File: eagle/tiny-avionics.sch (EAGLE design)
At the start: 60 parts, among them J1 USB-MICROB, J3 JST-PH-2-SMT-RA, U1 LP5907, U5 LTC1998, U6 ATMEGA32U4-AU, X1 8MHz

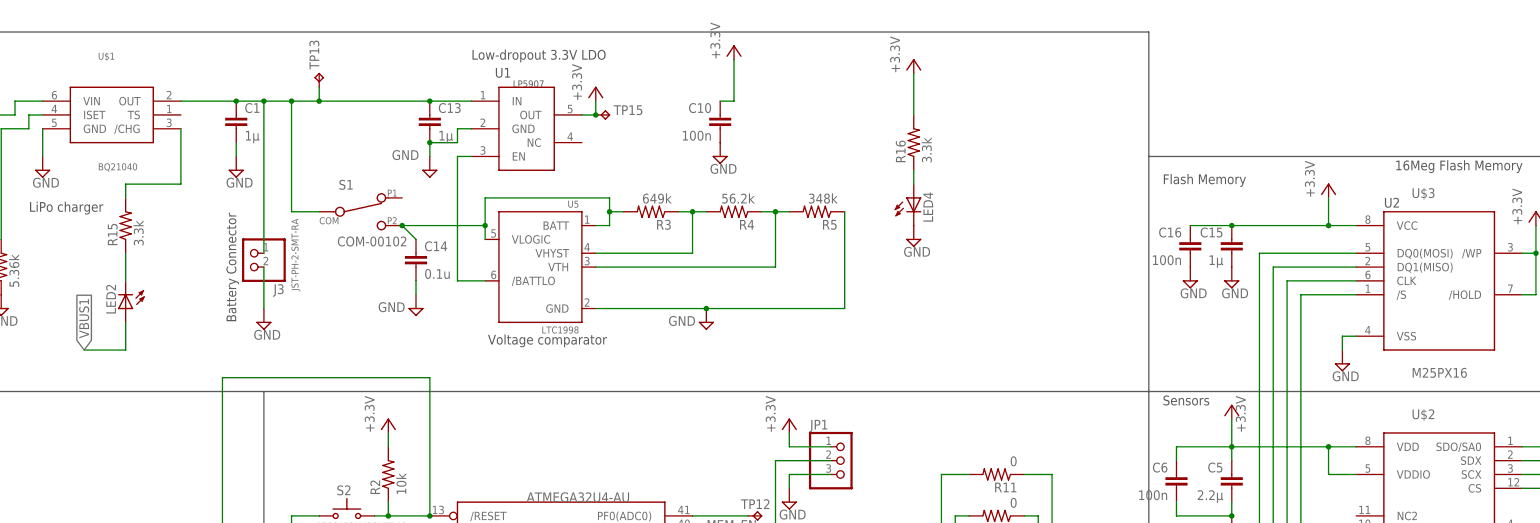
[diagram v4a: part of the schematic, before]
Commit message: Finished new board layout with no DRC errors.
It's a little smaller, but not much smaller.  Made an effort to spread out
components for easier assembly, however.  Layout is also much more
intuitive.
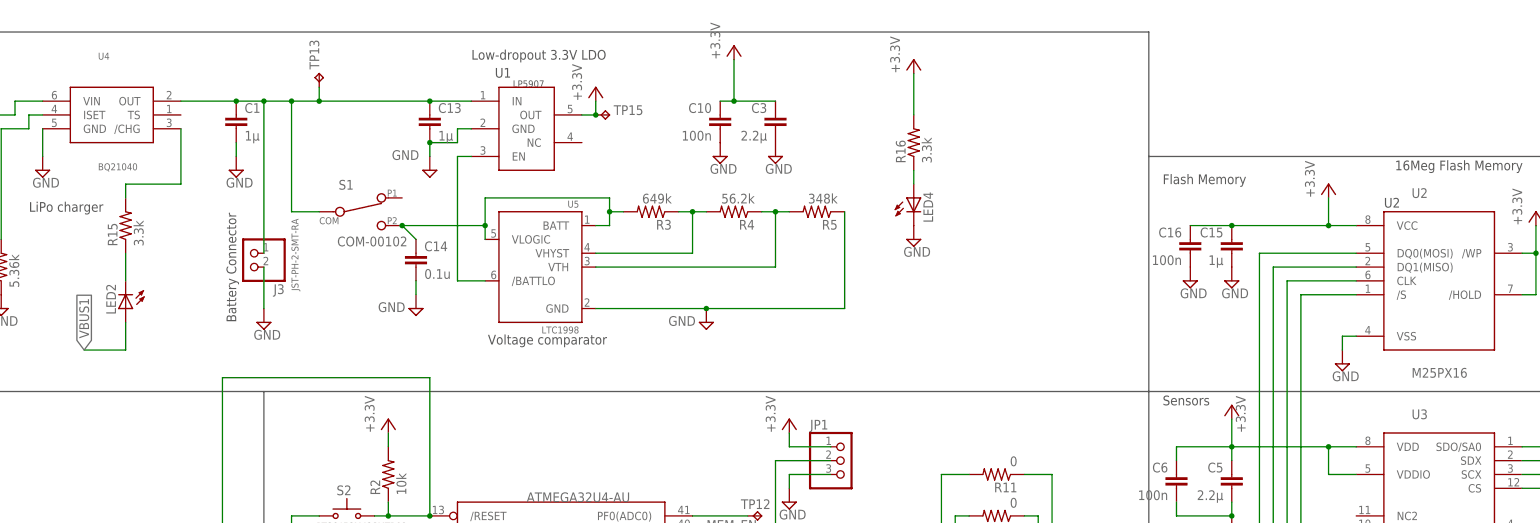
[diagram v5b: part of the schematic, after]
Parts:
- added C3: 2.2µ, rcl:C-EUC0603
- renumbered U$1 to U4, U$2 to U3, U$3 to U2
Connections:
- net GND: now also C3.2
- net VCC: now also C3.1
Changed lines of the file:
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@@
 <part name="TP15" library="testpad" deviceset="TP" device="TP08R"/>
 <part name="R17" library="rcl" deviceset="R-US_" device="R0603" value="0"/>
-<part name="U$1" library="tinyav-lib" deviceset="BQ21040" device=""/>
+<part name="U4" library="tinyav-lib" deviceset="BQ21040" device=""/>
 <part name="SUPPLY1" library="supply2" deviceset="GND" device=""/>
 <part name="R1" library="rcl" deviceset="R-US_" device="R0603" value="5.36k"/>
 <part name="SUPPLY3" library="supply2" deviceset="GND" device=""/>
-<part name="U$2" library="tinyav-lib" deviceset="LSM6DS3" device=""/>
+<part name="U3" library="tinyav-lib" deviceset="LSM6DS3" device=""/>
 <part name="SUPPLY7" library="supply2" deviceset="GND" device=""/>
 <part name="SUPPLY9" library="supply2" deviceset="GND" device=""/>
-<part name="U$3" library="tinyav-lib" deviceset="M25PX16" device=""/>
+<part name="U2" library="tinyav-lib" deviceset="M25PX16" device=""/>
 <part name="P+11" library="supply1" deviceset="VCC" device="" value="+3.3V"/>
 <part name="SUPPLY10" library="supply2" deviceset="GND" device=""/>
+<part name="C3" library="rcl" deviceset="C-EU" device="C0603" value="2.2µ"/>
+<part name="SUPPLY14" library="supply2" deviceset="GND" device=""/>
 </parts>
 <sheets>
@@
 <attribute name="VALUE" x="180.848" y="156.972" size="1.778" layer="96" rot="R180"/>
 </instance>
-<instance part="U$1" gate="BQ21040" x="68.58" y="248.92"/>
+<instance part="U4" gate="BQ21040" x="68.58" y="248.92"/>
 <instance part="SUPPLY1" gate="GND" x="55.88" y="238.76"/>
 <instance part="R1" gate="G$1" x="48.26" y="220.98" rot="R90"/>
 <instance part="SUPPLY3" gate="GND" x="48.26" y="213.36"/>
-<instance part="U$2" gate="G$1" x="312.42" y="175.26"/>
+<instance part="U3" gate="G$1" x="312.42" y="175.26"/>
 <instance part="SUPPLY7" gate="GND" x="292.1" y="154.94"/>
 <instance part="SUPPLY9" gate="GND" x="332.74" y="177.8"/>
-<instance part="U$3" gate="G$1" x="312.42" y="218.44"/>
+<instance part="U2" gate="G$1" x="312.42" y="218.44"/>
 <instance part="P+11" gate="VCC" x="330.2" y="231.14"/>
 <instance part="SUPPLY10" gate="GND" x="294.64" y="203.2"/>
+<instance part="C3" gate="G$1" x="190.5" y="248.92" rot="MR0"/>
+<instance part="SUPPLY14" gate="GND" x="190.5" y="241.3"/>
 </instances>
 <busses>
@@
 </segment>
 <segment>
-<pinref part="U$1" gate="BQ21040" pin="GND"/>
+<pinref part="U4" gate="BQ21040" pin="GND"/>
 <wire x1="55.88" y1="246.38" x2="55.88" y2="241.3" width="0.1524" layer="91"/>
 <pinref part="SUPPLY1" gate="GND" pin="GND"/>
@@
 </segment>
 <segment>
-<pinref part="U$2" gate="G$1" pin="GND"/>
+<pinref part="U3" gate="G$1" pin="GND"/>
 <wire x1="297.18" y1="165.1" x2="292.1" y2="165.1" width="0.1524" layer="91"/>
 <wire x1="292.1" y1="165.1" x2="292.1" y2="162.56" width="0.1524" layer="91"/>
-<pinref part="U$2" gate="G$1" pin="GND2"/>
+<pinref part="U3" gate="G$1" pin="GND2"/>
 <wire x1="292.1" y1="162.56" x2="297.18" y2="162.56" width="0.1524" layer="91"/>
 <wire x1="292.1" y1="162.56" x2="292.1" y2="157.48" width="0.1524" layer="91"/>
@@
 </segment>
 <segment>
-<pinref part="U$2" gate="G$1" pin="SDX"/>
+<pinref part="U3" gate="G$1" pin="SDX"/>
 <wire x1="327.66" y1="185.42" x2="332.74" y2="185.42" width="0.1524" layer="91"/>
 <wire x1="332.74" y1="185.42" x2="332.74" y2="182.88" width="0.1524" layer="91"/>
-<pinref part="U$2" gate="G$1" pin="SCX"/>
+<pinref part="U3" gate="G$1" pin="SCX"/>
 <wire x1="332.74" y1="182.88" x2="327.66" y2="182.88" width="0.1524" layer="91"/>
 <wire x1="332.74" y1="182.88" x2="332.74" y2="180.34" width="0.1524" layer="91"/>
@@
 <pinref part="SUPPLY10" gate="GND" pin="GND"/>
 <wire x1="294.64" y1="205.74" x2="294.64" y2="208.28" width="0.1524" layer="91"/>
-<pinref part="U$3" gate="G$1" pin="VSS"/>
+<pinref part="U2" gate="G$1" pin="VSS"/>
 <wire x1="294.64" y1="208.28" x2="297.18" y2="208.28" width="0.1524" layer="91"/>
+</segment>
+<segment>
+<pinref part="C3" gate="G$1" pin="2"/>
+<pinref part="SUPPLY14" gate="GND" pin="GND"/>
 </segment>
 </net>
@@
 <wire x1="210.82" y1="116.84" x2="210.82" y2="127" width="0.1524" layer="91"/>
 <junction x="210.82" y="127"/>
-<pinref part="U$2" gate="G$1" pin="SCL"/>
+<pinref part="U3" gate="G$1" pin="SCL"/>
 <wire x1="345.44" y1="165.1" x2="327.66" y2="165.1" width="0.1524" layer="91"/>
-<pinref part="U$3" gate="G$1" pin="CLK"/>
+<pinref part="U2" gate="G$1" pin="CLK"/>
 <wire x1="284.48" y1="218.44" x2="297.18" y2="218.44" width="0.1524" layer="91"/>
 </segment>
@@
 <wire x1="220.98" y1="119.38" x2="220.98" y2="129.54" width="0.1524" layer="91"/>
 <junction x="220.98" y="129.54"/>
-<pinref part="U$2" gate="G$1" pin="SDO/SA0"/>
+<pinref part="U3" gate="G$1" pin="SDO/SA0"/>
 <wire x1="350.52" y1="187.96" x2="327.66" y2="187.96" width="0.1524" layer="91"/>
 <wire x1="281.94" y1="129.54" x2="281.94" y2="220.98" width="0.1524" layer="91"/>
 <junction x="281.94" y="129.54"/>
-<pinref part="U$3" gate="G$1" pin="DQ1(MISO)"/>
+<pinref part="U2" gate="G$1" pin="DQ1(MISO)"/>
 <wire x1="281.94" y1="220.98" x2="297.18" y2="220.98" width="0.1524" layer="91"/>
 </segment>
@@
 <junction x="251.46" y="132.08"/>
 <wire x1="347.98" y1="132.08" x2="347.98" y2="162.56" width="0.1524" layer="91"/>
-<pinref part="U$2" gate="G$1" pin="SDA"/>
+<pinref part="U3" gate="G$1" pin="SDA"/>
 <wire x1="347.98" y1="162.56" x2="327.66" y2="162.56" width="0.1524" layer="91"/>
-<pinref part="U$3" gate="G$1" pin="DQ0(MOSI)"/>
+<pinref part="U2" gate="G$1" pin="DQ0(MOSI)"/>
 <wire x1="279.4" y1="223.52" x2="297.18" y2="223.52" width="0.1524" layer="91"/>
 </segment>
@@
 <wire x1="241.3" y1="182.88" x2="241.3" y2="172.72" width="0.1524" layer="91"/>
 <wire x1="241.3" y1="172.72" x2="266.7" y2="172.72" width="0.1524" layer="91"/>
-<pinref part="U$3" gate="G$1" pin="/S"/>
+<pinref part="U2" gate="G$1" pin="/S"/>
 <wire x1="287.02" y1="215.9" x2="297.18" y2="215.9" width="0.1524" layer="91"/>
 </segment>
@@
 <wire x1="238.76" y1="175.26" x2="238.76" y2="170.18" width="0.1524" layer="91"/>
 <wire x1="238.76" y1="170.18" x2="264.16" y2="170.18" width="0.1524" layer="91"/>
-<pinref part="U$2" gate="G$1" pin="CS"/>
+<pinref part="U3" gate="G$1" pin="CS"/>
 <wire x1="342.9" y1="180.34" x2="327.66" y2="180.34" width="0.1524" layer="91"/>
 <wire x1="342.9" y1="180.34" x2="342.9" y2="139.7" width="0.1524" layer="91"/>
@@
 <wire x1="182.88" y1="251.46" x2="182.88" y2="259.08" width="0.1524" layer="91"/>
 <pinref part="P+4" gate="VCC" pin="VCC"/>
+<pinref part="C3" gate="G$1" pin="1"/>
+<wire x1="182.88" y1="251.46" x2="190.5" y2="251.46" width="0.1524" layer="91"/>
+<junction x="182.88" y="251.46"/>
 </segment>
 <segment>
@@
 <wire x1="274.32" y1="187.96" x2="274.32" y2="193.04" width="0.1524" layer="91"/>
 <pinref part="P+1" gate="VCC" pin="VCC"/>
-<pinref part="U$2" gate="G$1" pin="VDD"/>
+<pinref part="U3" gate="G$1" pin="VDD"/>
 <wire x1="274.32" y1="187.96" x2="292.1" y2="187.96" width="0.1524" layer="91"/>
-<pinref part="U$2" gate="G$1" pin="VDDIO"/>
+<pinref part="U3" gate="G$1" pin="VDDIO"/>
 <wire x1="292.1" y1="187.96" x2="297.18" y2="187.96" width="0.1524" layer="91"/>
 <wire x1="297.18" y1="182.88" x2="292.1" y2="182.88" width="0.1524" layer="91"/>
@@
 <wire x1="266.7" y1="228.6" x2="274.32" y2="228.6" width="0.1524" layer="91"/>
 <junction x="274.32" y="228.6"/>
-<pinref part="U$3" gate="G$1" pin="VCC"/>
+<pinref part="U2" gate="G$1" pin="VCC"/>
 <wire x1="292.1" y1="228.6" x2="297.18" y2="228.6" width="0.1524" layer="91"/>
 <junction x="292.1" y="228.6"/>
@@
 </segment>
 <segment>
-<pinref part="U$3" gate="G$1" pin="/WP"/>
+<pinref part="U2" gate="G$1" pin="/WP"/>
 <wire x1="327.66" y1="223.52" x2="330.2" y2="223.52" width="0.1524" layer="91"/>
-<pinref part="U$3" gate="G$1" pin="/HOLD"/>
+<pinref part="U2" gate="G$1" pin="/HOLD"/>
 <wire x1="327.66" y1="215.9" x2="330.2" y2="215.9" width="0.1524" layer="91"/>
 <wire x1="330.2" y1="215.9" x2="330.2" y2="223.52" width="0.1524" layer="91"/>
@@
 <wire x1="38.1" y1="248.92" x2="50.8" y2="248.92" width="0.1524" layer="91"/>
 <wire x1="50.8" y1="248.92" x2="50.8" y2="251.46" width="0.1524" layer="91"/>
-<pinref part="U$1" gate="BQ21040" pin="VIN"/>
+<pinref part="U4" gate="BQ21040" pin="VIN"/>
 <wire x1="50.8" y1="251.46" x2="55.88" y2="251.46" width="0.1524" layer="91"/>
 </segment>
@@
 <wire x1="106.68" y1="251.46" x2="106.68" y2="254" width="0.1524" layer="91"/>
 <junction x="106.68" y="251.46"/>
-<pinref part="U$1" gate="BQ21040" pin="OUT"/>
+<pinref part="U4" gate="BQ21040" pin="OUT"/>
 <wire x1="81.28" y1="251.46" x2="91.44" y2="251.46" width="0.1524" layer="91"/>
 <junction x="91.44" y="251.46"/>
@@
 <wire x1="71.12" y1="233.68" x2="71.12" y2="236.22" width="0.1524" layer="91"/>
 <wire x1="71.12" y1="236.22" x2="81.28" y2="236.22" width="0.1524" layer="91"/>
-<pinref part="U$1" gate="BQ21040" pin="/CHG"/>
+<pinref part="U4" gate="BQ21040" pin="/CHG"/>
 <wire x1="81.28" y1="236.22" x2="81.28" y2="246.38" width="0.1524" layer="91"/>
 </segment>
@@
 <wire x1="48.26" y1="246.38" x2="53.34" y2="246.38" width="0.1524" layer="91"/>
 <wire x1="53.34" y1="246.38" x2="53.34" y2="248.92" width="0.1524" layer="91"/>
-<pinref part="U$1" gate="BQ21040" pin="ISET"/>
+<pinref part="U4" gate="BQ21040" pin="ISET"/>
 <wire x1="53.34" y1="248.92" x2="55.88" y2="248.92" width="0.1524" layer="91"/>
 </segment>
@@
 <wire x1="175.26" y1="101.6" x2="340.36" y2="101.6" width="0.1524" layer="91"/>
 <wire x1="340.36" y1="101.6" x2="340.36" y2="172.72" width="0.1524" layer="91"/>
-<pinref part="U$2" gate="G$1" pin="INT1"/>
+<pinref part="U3" gate="G$1" pin="INT1"/>
 <wire x1="340.36" y1="172.72" x2="327.66" y2="172.72" width="0.1524" layer="91"/>
 </segment>
@@
 <wire x1="175.26" y1="104.14" x2="337.82" y2="104.14" width="0.1524" layer="91"/>
 <wire x1="337.82" y1="104.14" x2="337.82" y2="170.18" width="0.1524" layer="91"/>
-<pinref part="U$2" gate="G$1" pin="INT2"/>
+<pinref part="U3" gate="G$1" pin="INT2"/>
 <wire x1="337.82" y1="170.18" x2="327.66" y2="170.18" width="0.1524" layer="91"/>
 </segment>

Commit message: Added SMD crystal device and replaced on board
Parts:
- X1: device IQD-Frequency-Products:CRYSTALS-NOGND-HC49/4H -> tinyav-lib:CRYSTAL-NOGND-SMD
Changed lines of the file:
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@@
 <part name="SUPPLY17" library="supply2" deviceset="GND" device=""/>
 <part name="P+5" library="supply1" deviceset="VCC" device="" value="+3.3V"/>
-<part name="X1" library="IQD-Frequency-Products" deviceset="CRYSTALS-NOGND" device="-HC49/4H" value="8MHz">
+<part name="X1" library="tinyav-lib" deviceset="CRYSTAL-NOGND-SMD" device="" value="8MHz">
 <attribute name="MPN" value="ATS080B"/>
 <attribute name="VENDOR" value="DIGIKEY"/>

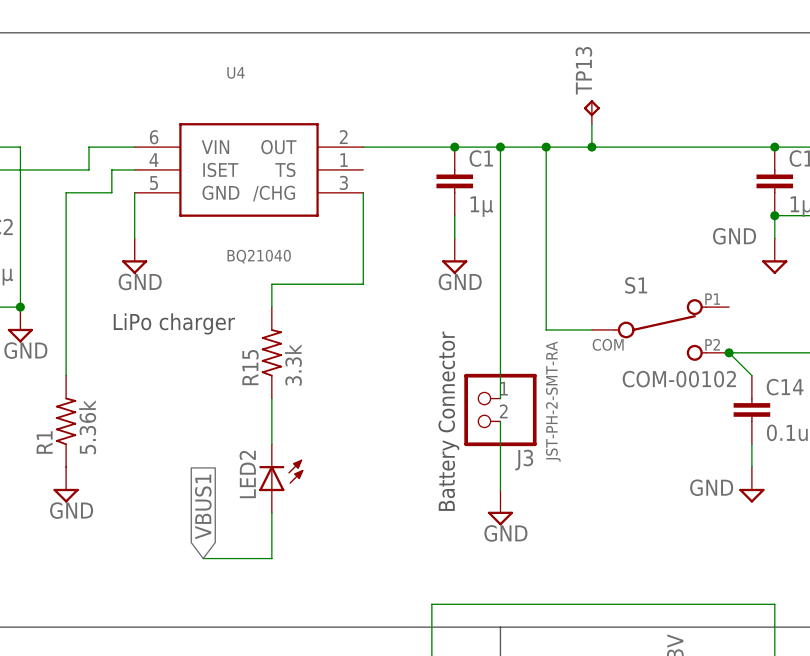
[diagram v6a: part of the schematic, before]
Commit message: Added thermistor to bottom of board
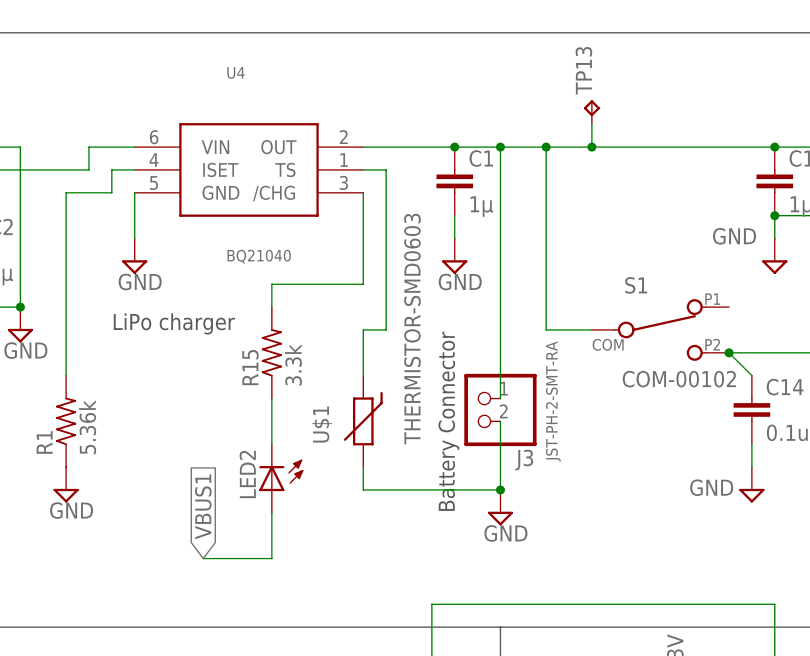
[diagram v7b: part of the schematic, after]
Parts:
- added U$1: THERMISTOR-SMD0603, tinyav-lib:THERMISTOR-SMD0603
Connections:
- new net N$9: U$1.1, U4.TS
- net GND: now also U$1.2
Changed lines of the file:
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@@
 <part name="C3" library="rcl" deviceset="C-EU" device="C0603" value="2.2µ"/>
 <part name="SUPPLY14" library="supply2" deviceset="GND" device=""/>
+<part name="U$1" library="tinyav-lib" deviceset="THERMISTOR-SMD" device="0603"/>
 </parts>
 <sheets>
@@
 <instance part="C3" gate="G$1" x="190.5" y="248.92" rot="MR0"/>
 <instance part="SUPPLY14" gate="GND" x="190.5" y="241.3"/>
+<instance part="U$1" gate="G$1" x="81.28" y="220.98" rot="R90"/>
 </instances>
 <busses>
@@
 <pinref part="SUPPLY2" gate="GND" pin="GND"/>
 <wire x1="96.52" y1="220.98" x2="96.52" y2="213.36" width="0.1524" layer="91"/>
+<pinref part="U$1" gate="G$1" pin="2"/>
+<wire x1="81.28" y1="215.9" x2="81.28" y2="213.36" width="0.1524" layer="91"/>
+<wire x1="81.28" y1="213.36" x2="96.52" y2="213.36" width="0.1524" layer="91"/>
+<junction x="96.52" y="213.36"/>
 </segment>
 <segment>
@@
 </segment>
 </net>
+<net name="N$9" class="0">
+<segment>
+<pinref part="U4" gate="BQ21040" pin="TS"/>
+<wire x1="81.28" y1="248.92" x2="83.82" y2="248.92" width="0.1524" layer="91"/>
+<wire x1="83.82" y1="248.92" x2="83.82" y2="231.14" width="0.1524" layer="91"/>
+<wire x1="83.82" y1="231.14" x2="81.28" y2="231.14" width="0.1524" layer="91"/>
+<pinref part="U$1" gate="G$1" pin="1"/>
+<wire x1="81.28" y1="231.14" x2="81.28" y2="226.06" width="0.1524" layer="91"/>
+</segment>
+</net>
